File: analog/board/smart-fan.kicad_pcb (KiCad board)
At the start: 2 copper layers, 31 parts, among them J1 Conn_01x03_MountingPin, J2 Barrel_Jack, J3 Screw_Terminal_01x02, J4 Conn_01x03_Male, Q1 BC817, Q2 Q_PMOS_GSD, Q3 Q_PMOS_GSD, Q4 BC817, U1 MCP602, U2 AMS1117-5.0, U3 NE555P

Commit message: Working on analog board layout
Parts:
- J1: value Conn_01x03_MountingPin -> TEMP_In; footprint Connector_Pin127mm:PinHeader_1x03_P1.27mm_Vertical -> Connector_PinHeader_1.27mm:PinHeader_1x03_P1.27mm_Vertical
- J2: value Barrel_Jack -> 12V_PWR
- J3: value Screw_Terminal_01x02 -> 12V_In; footprint Connector_PinSocket254mm:PinSocket_1x02_P2.54mm_Vertical -> Connector_PinSocket_2.54mm:PinSocket_1x02_P2.54mm_Vertical
- J4: value Conn_01x03_Male -> FAN_Out; footprint Connector_Pin127mm:PinHeader_1x03_P1.27mm_Vertical -> Connector_JST:JST_EH_B3B-EH-A_1x03_P2.50mm_Vertical
- RV1: footprint Resistor_SMD:R_0805_2012Metric_Pad1.15x1.40mm_HandSolder -> Potentiometer_THT:Potentiometer_Bourns_3266Y_Vertical
- U1: footprint Package_SO:SOIC-8_3.9x4.9mm_P1.27mm -> Package_SO:SOIC-8_5.275x5.275mm_P1.27mm
- U3: footprint Package_DIP:DIP-8_W7.62mm -> Package_SO:SOIC-8_5.275x5.275mm_P1.27mm
- moved R11 39.6 mm to (22.9, 39.8), turned to 270 degrees
- moved J3 38.1 mm to (13.8, 30.1)
- moved R3 35.3 mm to (30.2, 29.5), turned to 270 degrees
- moved Q1 35.2 mm to (29.4, 15.6), turned to 180 degrees
- moved Q4 35.1 mm to (18.9, 39.8), turned to 270 degrees
- moved Q3 32.1 mm to (30.2, 39.8), turned to 270 degrees
- moved C3 28.6 mm to (30.2, 24.4), turned to 270 degrees
- moved Q2 28.3 mm to (54.0, 21.0), turned to 90 degrees
- moved J2 27.5 mm to (14.5, 18.8), turned to 90 degrees
- moved R6 26.9 mm to (30.2, 19.9), turned to 270 degrees
- moved J1 26.4 mm to (13.8, 39.9), turned to 180 degrees
- moved R1 25.5 mm to (34.3, 15.4)
- moved C7 24.4 mm to (34.4, 26.0)
- moved U3 23.1 mm to (37.1, 20.1)
- moved R4 22.6 mm to (40.0, 15.4), turned to 180 degrees
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
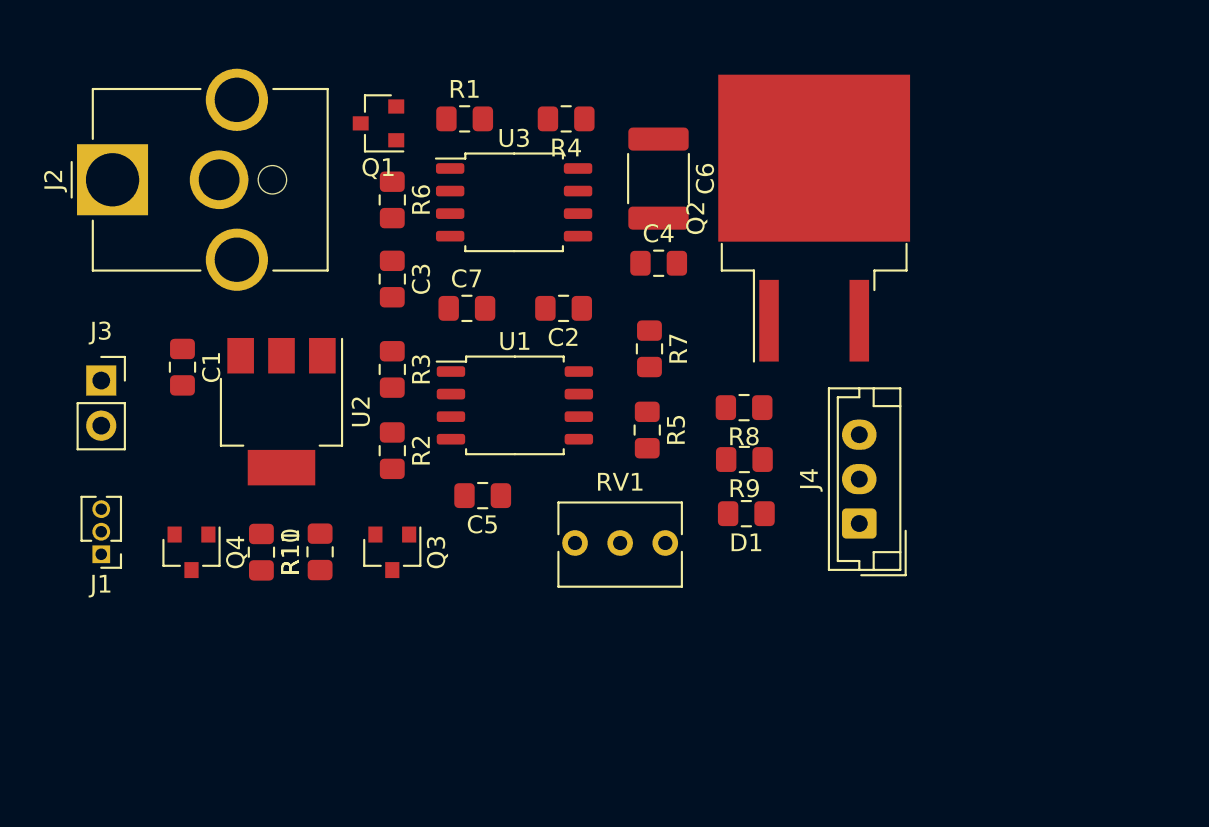
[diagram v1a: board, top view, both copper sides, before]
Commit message: Improving board layout
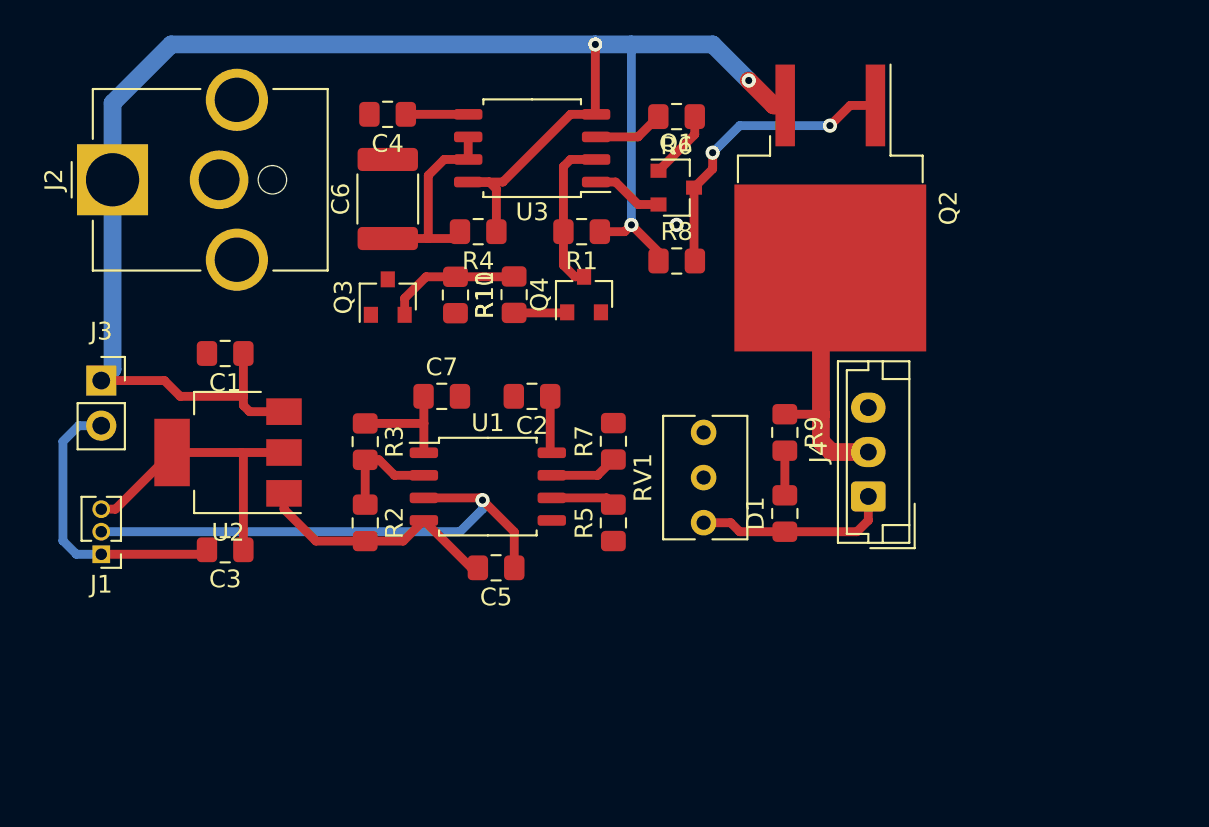
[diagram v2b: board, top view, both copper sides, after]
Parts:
- moved Q4 26.4 mm to (41.0, 25.3), turned to 90 degrees
- moved R11 20.3 mm to (37.1, 25.3), turned to 90 degrees
- moved C3 17.9 mm to (20.8, 39.6), turned to 180 degrees
- moved C4 17.4 mm to (30.0, 15.1), turned to 180 degrees
- moved Q1 17.1 mm to (46.2, 19.2), turned to 0 degrees
- moved R6 16.7 mm to (46.2, 15.2), turned to 180 degrees
- moved R10 16.3 mm to (33.8, 25.3), turned to 270 degrees
- moved C6 15.3 mm to (30.0, 19.9), turned to 90 degrees
- moved Q3 14.4 mm to (30.0, 25.4), turned to 90 degrees
- moved R1 9.15 mm to (40.9, 21.7), turned to 180 degrees
- moved R8 9.08 mm to (46.2, 23.4), turned to 0 degrees
- moved R4 8.05 mm to (35.1, 21.7)
- moved RV1 6.59 mm to (47.8, 33.0), turned to 90 degrees
- moved R7 5.59 mm to (42.7, 33.5), turned to 90 degrees
- moved R5 5.56 mm to (42.7, 38.1), turned to 90 degrees
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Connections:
- D1 pad 1: Net-(D1-Pad1) -> GND
- J4 pad 2: Net-(D1-Pad2) -> Net-(J4-Pad2)
- Q2 pad 2: Net-(D1-Pad2) -> Net-(J4-Pad2)
- R9 pad 1: Net-(D1-Pad1) -> Net-(J4-Pad2)
- R9 pad 2: GND -> Net-(D1-Pad2)
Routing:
- net +12V: track 0.00 -> 101.9 mm, vias 0 -> 3
- net GND: track 0.00 -> 45.9 mm
- net /TMP_IN: track 0.00 -> 30.4 mm, vias 0 -> 1
- net +5V: track 0.00 -> 20.3 mm
- net Net-(Q1-Pad3): track 0.00 -> 16.8 mm, vias 0 -> 2
- net Net-(J4-Pad2): track 0.00 -> 14.4 mm
- net Net-(C6-Pad1): track 0.00 -> 11.7 mm
- net Trigger: track 0.00 -> 8.99 mm
- net Net-(Q3-Pad2): track 0.00 -> 7.60 mm
- net Net-(C7-Pad1): track 0.00 -> 6.48 mm
- net Net-(R2-Pad1): track 0.00 -> 6.18 mm
- net Net-(R6-Pad2): track 0.00 -> 3.98 mm
- net Net-(Q1-Pad1): track 0.00 -> 3.89 mm
- net Net-(Q3-Pad1): track 0.00 -> 3.84 mm
- net Net-(R5-Pad2): track 0.00 -> 3.63 mm
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
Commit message: Improving board layout
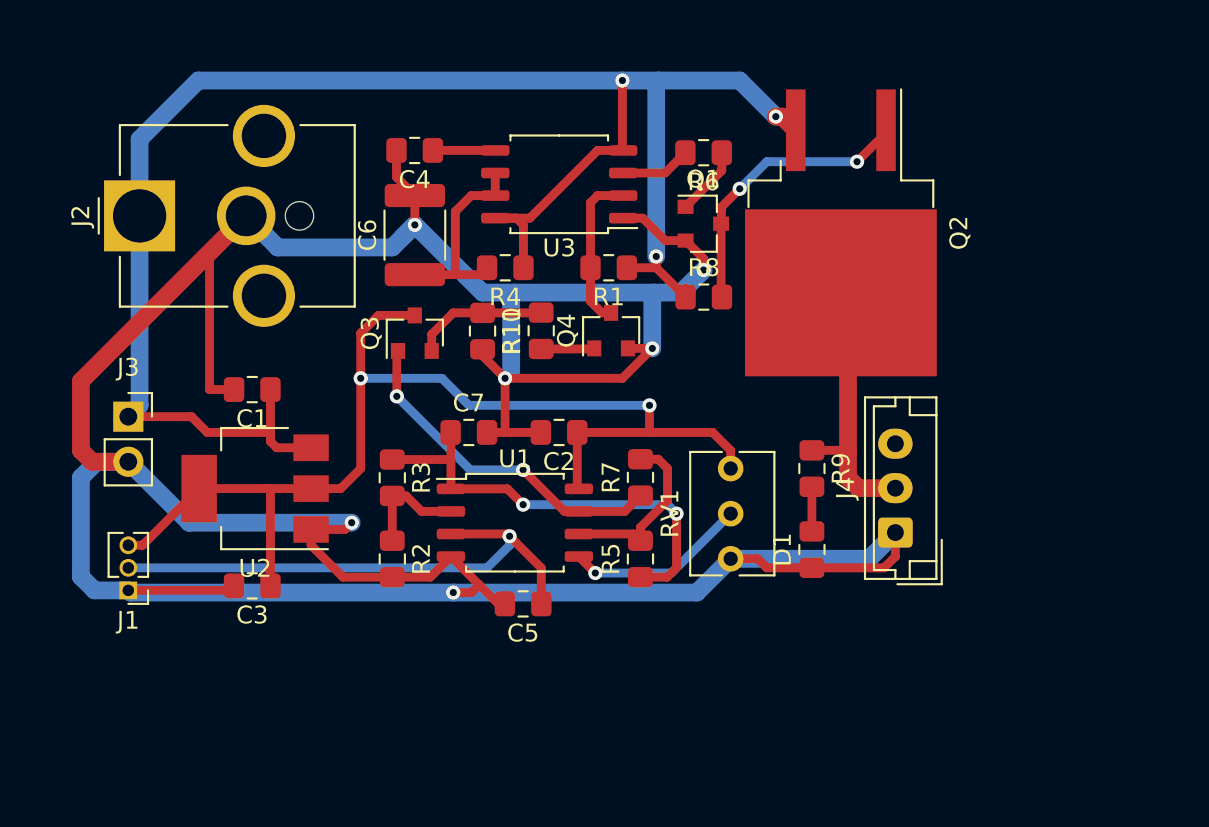
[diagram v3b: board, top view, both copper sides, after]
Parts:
- moved C2 2.54 mm to (39.6, 33.0)
- moved D1 2.54 mm to (53.8, 39.6)
- moved R7 2.54 mm to (44.2, 35.6)
- moved U1 2.54 mm to (37.1, 38.1)
- moved R3 2.54 mm to (30.2, 35.6)
- moved C1 2.54 mm to (22.3, 30.6)
- moved J3 2.54 mm to (15.4, 32.1)
- moved Q4 2.54 mm to (42.5, 27.3)
- moved R1 2.54 mm to (42.4, 23.7)
- moved R10 2.54 mm to (35.3, 27.3)
- moved R4 2.54 mm to (36.6, 23.7)
- moved R8 2.54 mm to (47.8, 25.4)
- moved U3 2.54 mm to (39.6, 19.1)
- moved J2 2.54 mm to (16.0, 20.8)
- moved C7 2.54 mm to (34.5, 33.0)
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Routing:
- net GND: track 45.9 -> 205.3 mm, vias 0 -> 6
- net +5V: track 20.3 -> 63.2 mm, vias 0 -> 2
- net Net-(C7-Pad1): track 6.48 -> 25.1 mm, vias 0 -> 2
- net Net-(Q3-Pad1): track 3.84 -> 19.4 mm, vias 0 -> 2
- net Net-(RV1-Pad2): track 0.00 -> 10.3 mm, vias 0 -> 1
- net Net-(R5-Pad2): track 3.63 -> 10.1 mm
- net Net-(Q1-Pad3): track 16.8 -> 15.4 mm
- net +12V: track 101.9 -> 101.0 mm
- net (no net): vias 1 -> 0

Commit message: Board layout complete with ground planes and mounting holes
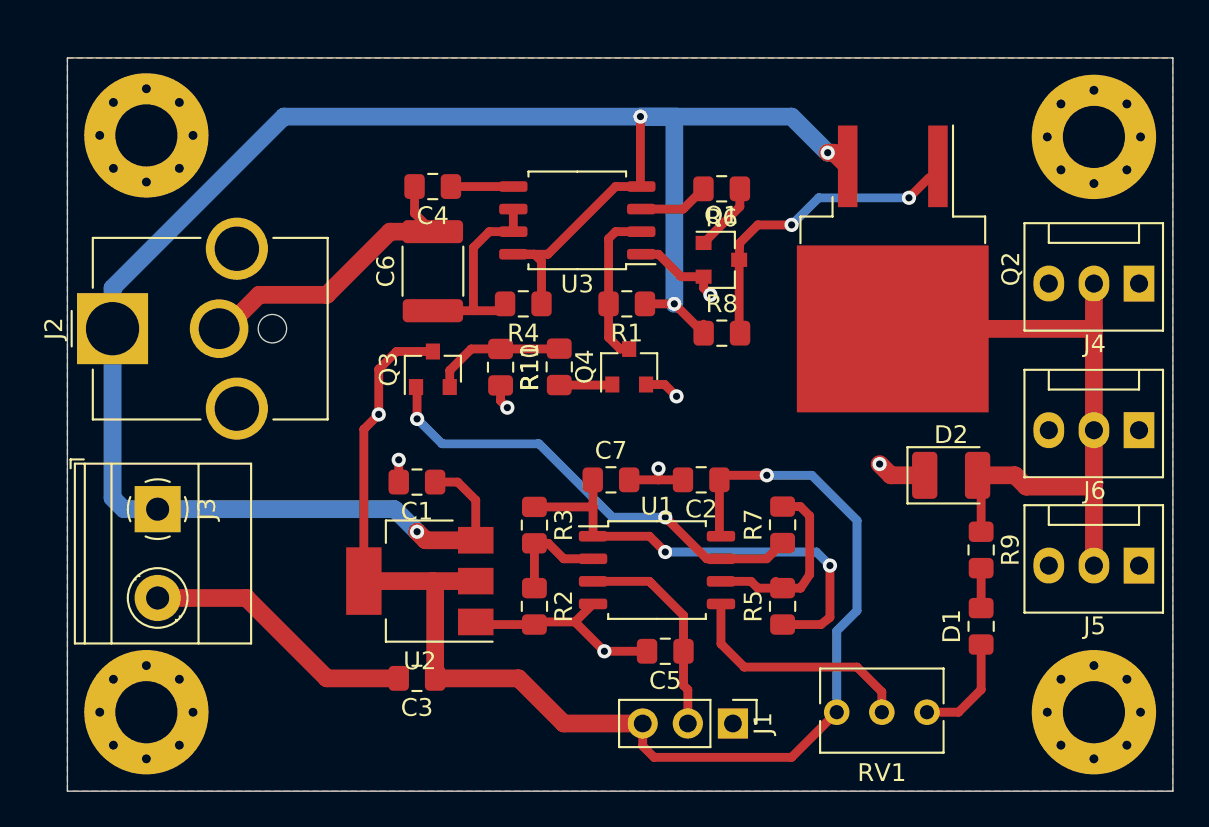
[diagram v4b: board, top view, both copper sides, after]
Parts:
- added D2: D_Schottky, Diode_SMD:D_1210_3225Metric_Pad1.42x2.65mm_HandSolder, F.Cu at (61.7, 35.4)
- added J5: FAN_Out, Connector:FanPinHeader_1x03_P2.54mm_Vertical, F.Cu at (72.3, 40.5)
- added J6: FAN_Out, Connector:FanPinHeader_1x03_P2.54mm_Vertical, F.Cu at (72.3, 32.9)
- added REF**: MountingHole_3.5mm_Pad_Via, MountingHole:MountingHole_3.5mm_Pad_Via, F.Cu at (16.4, 48.8)
- added REF**: MountingHole_3.5mm_Pad_Via, MountingHole:MountingHole_3.5mm_Pad_Via, F.Cu at (69.7, 48.8)
- added REF**: MountingHole_3.5mm_Pad_Via, MountingHole:MountingHole_3.5mm_Pad_Via, F.Cu at (69.7, 16.4)
- added REF**: MountingHole_3.5mm_Pad_Via, MountingHole:MountingHole_3.5mm_Pad_Via, F.Cu at (16.4, 16.3)
- J1: footprint Connector_PinHeader_1.27mm:PinHeader_1x03_P1.27mm_Vertical -> Connector_PinHeader_2.54mm:PinHeader_1x03_P2.54mm_Vertical
- J3: footprint Connector_PinSocket_2.54mm:PinSocket_1x02_P2.54mm_Vertical -> TerminalBlock_Phoenix:TerminalBlock_Phoenix_MKDS-1,5-2_1x02_P5.00mm_Horizontal
- J4: footprint Connector_JST:JST_EH_B3B-EH-A_1x03_P2.50mm_Vertical -> Connector:FanPinHeader_1x03_P2.54mm_Vertical
- moved J1 34.9 mm to (49.4, 49.4), turned to 270 degrees
- moved J4 19.6 mm to (72.3, 24.6), turned to 180 degrees
- moved RV1 15.0 mm to (55.2, 48.8), turned to 180 degrees
- moved C1 10.6 mm to (31.6, 35.8)
- moved C3 10.6 mm to (31.6, 46.9)
- moved U2 10.6 mm to (31.8, 41.4)
- moved R9 10.6 mm to (63.4, 39.6)
- moved D1 10.5 mm to (63.4, 43.9)
- moved C5 8.43 mm to (45.6, 45.3)
- moved R5 8.43 mm to (52.2, 42.8)
- moved R7 8.43 mm to (52.2, 38.2)
- moved C7 8.43 mm to (42.5, 35.7)
- moved R2 8.43 mm to (38.2, 42.8)
- moved U1 8.43 mm to (45.1, 40.8)
- moved C2 8.43 mm to (47.6, 35.7)
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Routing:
- net GND: track 205.3 -> 67.4 mm, vias 6 -> 7
- net Net-(D2-Pad2): track 14.4 -> 38.0 mm
- net /TMP_IN: track 30.4 -> 12.1 mm, vias 1 -> 0
- net +12V: track 101.0 -> 118.6 mm, vias 3 -> 4
- net +5V: track 63.2 -> 77.4 mm
- net Net-(Q3-Pad1): track 19.4 -> 26.1 mm
- net Net-(RV1-Pad2): track 10.3 -> 13.6 mm, vias 1 -> 0
- net Net-(Q1-Pad3): track 15.4 -> 17.3 mm
- net Net-(C7-Pad1): track 25.1 -> 26.2 mm
- net Net-(R5-Pad2): track 10.1 -> 11.1 mm
- added copper zone on B.Cu, net GND
- added copper zone on F.Cu, net GND
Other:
- board outline added: 62.2 x 41.3 mm
